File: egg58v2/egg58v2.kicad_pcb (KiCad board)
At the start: 2 copper layers, 146.1 x 146 mm, 32 parts, among them J1 AudioJack4, SW11 SW_PUSH_LED, SW12 SW_PUSH_LED, SW13 SW_PUSH_LED, SW14 SW_PUSH_LED, SW15 SW_PUSH_LED, SW16 SW_PUSH_LED, SW21 SW_PUSH_LED, SW22 SW_PUSH_LED, SW23 SW_PUSH_LED, SW24 SW_PUSH_LED, SW25 SW_PUSH_LED, SW26 SW_PUSH_LED, SW31 SW_PUSH_LED, SW32 SW_PUSH_LED, SW33 SW_PUSH_LED, SW34 SW_PUSH_LED, SW35 SW_PUSH_LED, SW36 SW_PUSH_LED, SW41 SW_PUSH_LED, SW42 SW_PUSH_LED, SW43 SW_PUSH_LED, SW44 SW_PUSH_LED, SW45 SW_PUSH_LED, SW46 SW_PUSH_LED, SW52 SW_PUSH_LED, SW53 SW_PUSH_LED, SW54 SW_PUSH_LED, SW55 SW_PUSH_LED, SW56 SW_PUSH_LED, U1 Elite-C

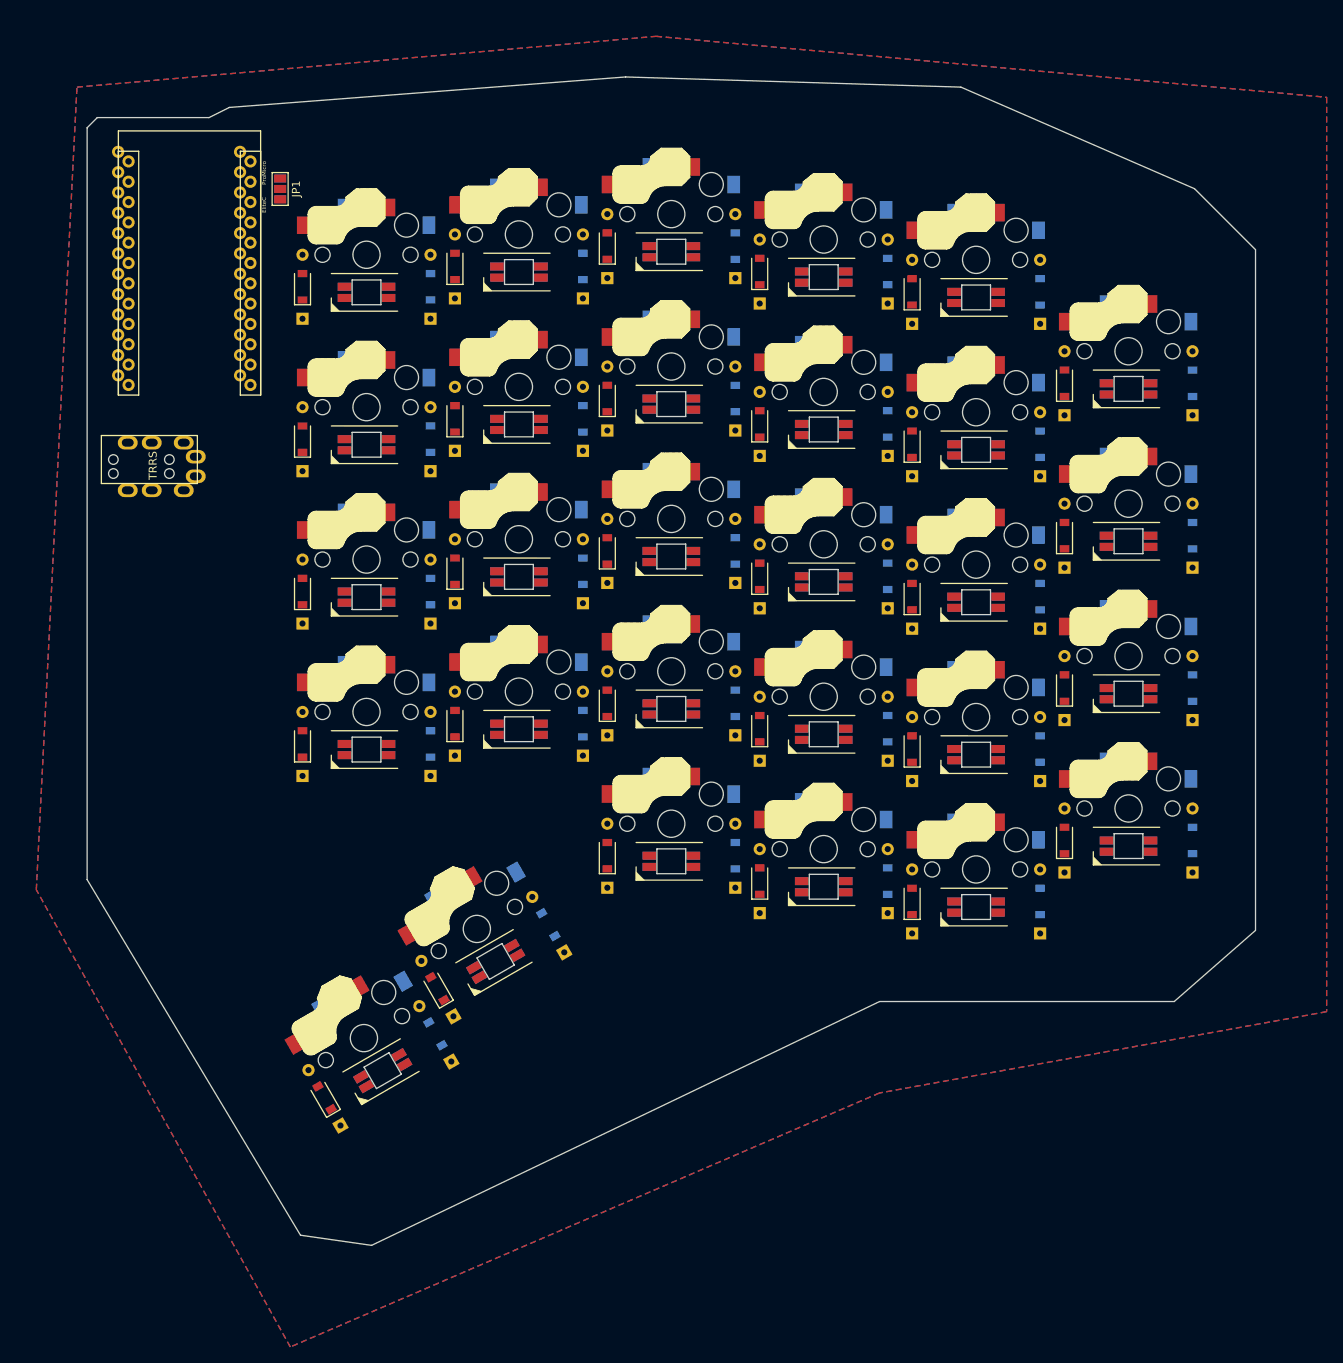
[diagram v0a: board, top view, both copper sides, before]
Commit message: update to choc switch spacing, add logo
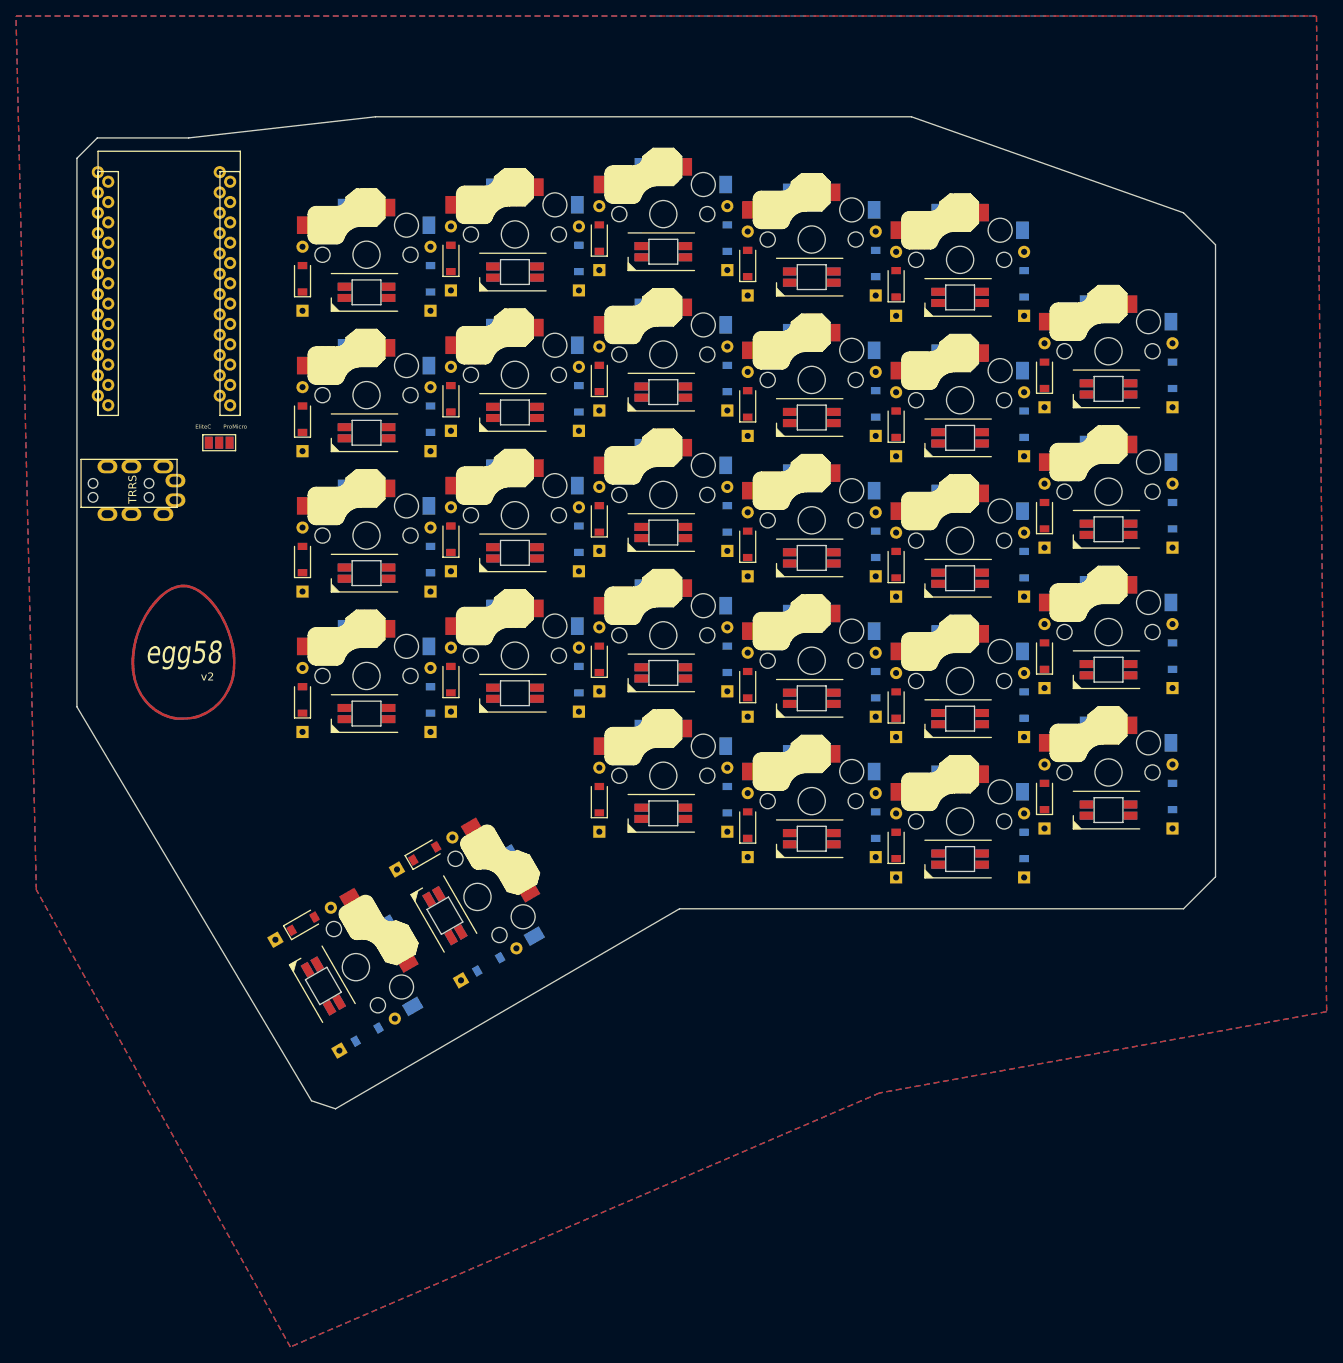
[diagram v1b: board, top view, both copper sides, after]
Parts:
- added G***: LOGO, egg58v2:egg58logo, F.Cu at (120.0, 105.0)
- moved JP1 32.6 mm to (124.5, 78.7), turned to 180 degrees
- moved SW56 8.93 mm to (141.5, 144.3), turned to 300 degrees
- moved SW52 6.32 mm to (217.1, 126.1)
- moved SW53 6.18 mm to (198.5, 123.5)
- moved SW54 6.08 mm to (180.0, 120.4)
- moved SW41 5.15 mm to (235.6, 120.0)
- moved SW42 4.92 mm to (217.1, 108.5)
- moved SW43 4.74 mm to (198.5, 106.0)
- moved SW44 4.61 mm to (180.0, 102.8)
- moved SW45 4.53 mm to (161.4, 105.4)
- moved SW46 4.50 mm to (142.9, 107.9)
- moved SW55 4.00 mm to (156.7, 135.5), turned to 300 degrees
- moved J1 3.92 mm to (107.2, 83.8)
- moved SW31 3.91 mm to (235.6, 102.4)
- moved SW32 3.61 mm to (217.1, 91.0)
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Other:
- board size 146.1 x 146 mm -> 142.3 x 124 mm

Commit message: footprint updates
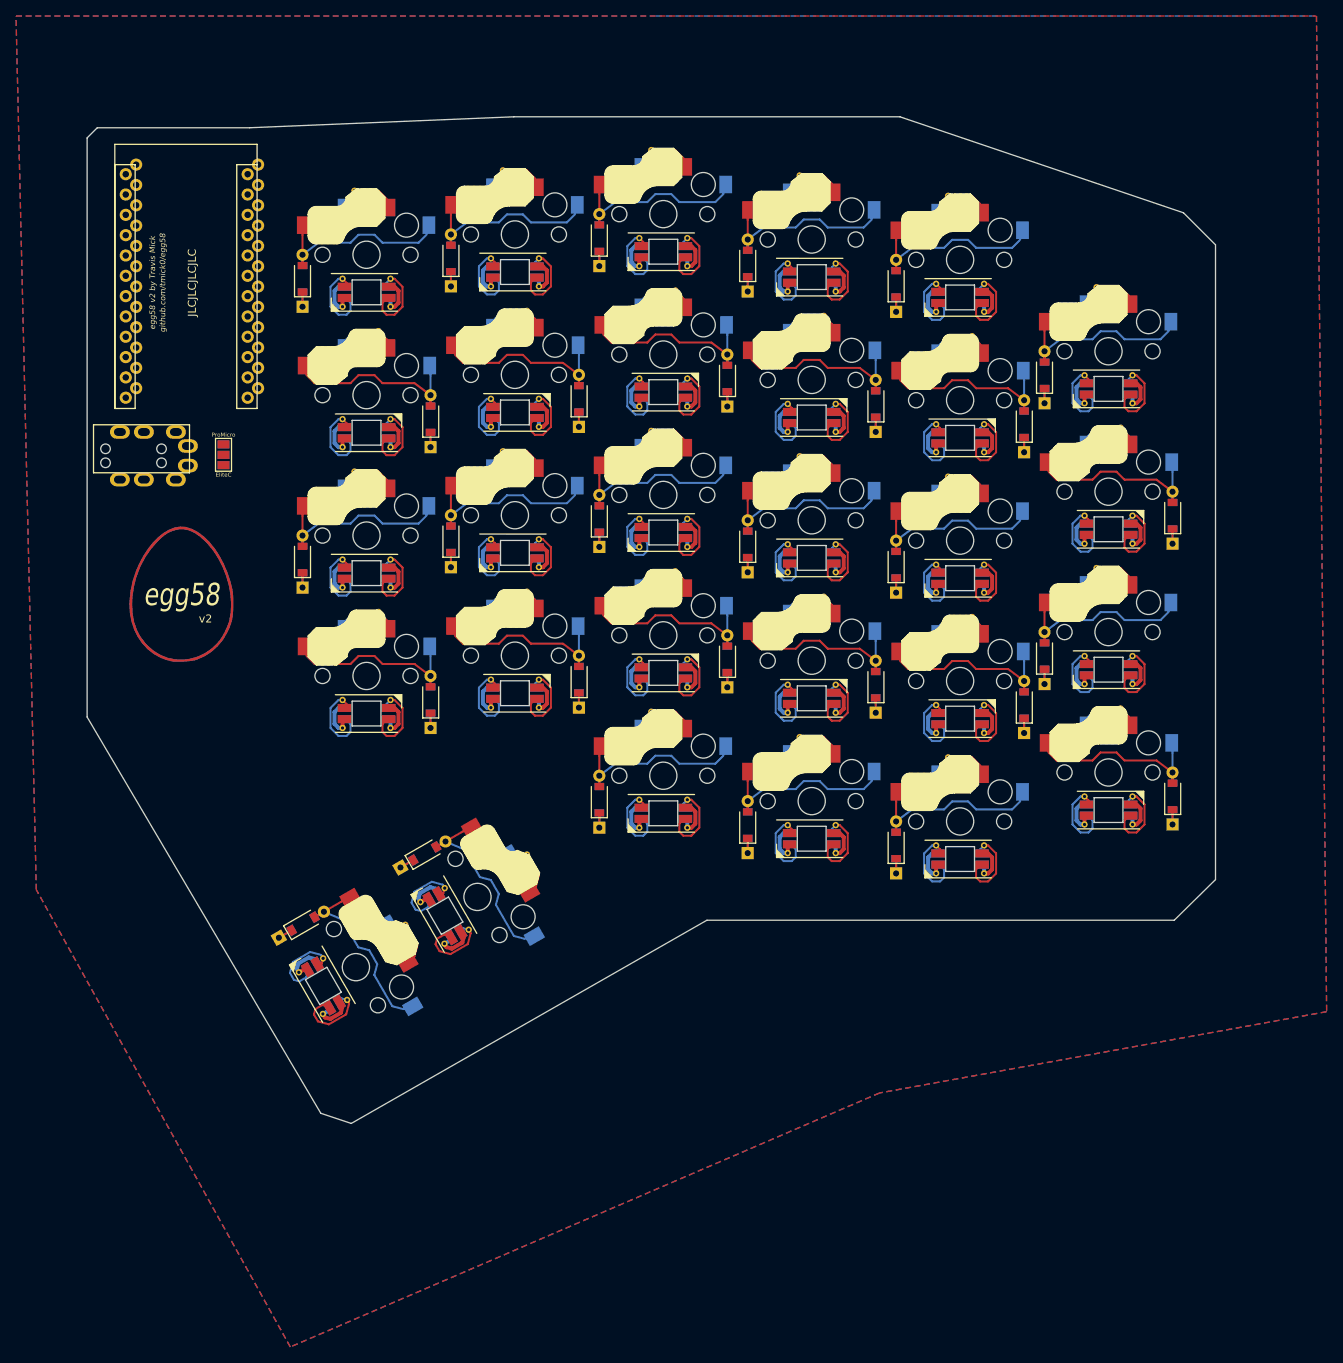
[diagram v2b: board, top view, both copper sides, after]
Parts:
- added REF**: egg58url, egg58v2:egg58url, F.Cu at (116.2, 58.8)
- SW21, SW22, SW23, SW24, SW25, SW26, SW41, SW42, SW43, SW44, SW45, SW46, U1: moved to B.Cu
- moved G*** 7.25 mm to (119.8, 97.8)
- moved J1 4.59 mm to (108.8, 79.5)
- moved U1 2.57 mm to (120.5, 58.8), turned to 180 degrees
- moved JP1 1.60 mm to (125.0, 80.2), turned to 270 degrees
- turned SW21 to 180 degrees
- turned SW22 to 180 degrees
- turned SW23 to 180 degrees
- turned SW24 to 180 degrees
- turned SW25 to 180 degrees
- turned SW26 to 180 degrees
- turned SW41 to 180 degrees
- turned SW42 to 180 degrees
- turned SW43 to 180 degrees
- turned SW44 to 180 degrees
- turned SW45 to 180 degrees
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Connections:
- SW11 pad 5: Net-(SW11-Pad5) -> Col1
- SW11 pad 7: Net-(SW11-Pad6) -> Row1
- SW12 pad 5: Net-(SW12-Pad5) -> Col2
- SW12 pad 7: Net-(SW12-Pad6) -> Row1
- SW13 pad 5: Net-(SW13-Pad5) -> Col3
- SW13 pad 7: Net-(SW13-Pad6) -> Row1
- SW14 pad 5: Net-(SW14-Pad5) -> Col4
- SW14 pad 7: Net-(SW14-Pad6) -> Row1
- SW15 pad 5: Net-(SW15-Pad5) -> Col5
- SW15 pad 7: Net-(SW15-Pad6) -> Row1
- SW16 pad 5: Net-(SW16-Pad5) -> Col6
- SW16 pad 7: Net-(SW16-Pad6) -> Row1
- SW21 pad 5: Net-(SW21-Pad5) -> Col1
- SW21 pad 7: Net-(SW21-Pad6) -> Row2
- SW22 pad 5: Net-(SW22-Pad5) -> Col2
- SW22 pad 7: Net-(SW22-Pad6) -> Row2
- SW23 pad 5: Net-(SW23-Pad5) -> Col3
- SW23 pad 7: Net-(SW23-Pad6) -> Row2
- SW24 pad 5: Net-(SW24-Pad5) -> Col4
- SW24 pad 7: Net-(SW24-Pad6) -> Row2
- SW25 pad 5: Net-(SW25-Pad5) -> Col5
- SW25 pad 7: Net-(SW25-Pad6) -> Row2
- SW26 pad 5: Net-(SW26-Pad5) -> Col6
- SW26 pad 7: Net-(SW26-Pad6) -> Row2
- SW31 pad 5: Net-(SW31-Pad5) -> Col1
- SW31 pad 7: Net-(SW31-Pad6) -> Row3
- SW32 pad 5: Net-(SW32-Pad5) -> Col2
- SW32 pad 7: Net-(SW32-Pad6) -> Row3
- SW33 pad 5: Net-(SW33-Pad5) -> Col3
- SW33 pad 7: Net-(SW33-Pad6) -> Row3
- SW34 pad 5: Net-(SW34-Pad5) -> Col4
- SW34 pad 7: Net-(SW34-Pad6) -> Row3
- SW35 pad 5: Net-(SW35-Pad5) -> Col5
- SW35 pad 7: Net-(SW35-Pad6) -> Row3
- SW36 pad 5: Net-(SW36-Pad5) -> Col6
- SW36 pad 7: Net-(SW36-Pad6) -> Row3
- SW41 pad 7: Net-(SW41-Pad6) -> Row4
- SW42 pad 5: Net-(SW42-Pad5) -> Col2
- SW42 pad 7: Net-(SW42-Pad6) -> Row4
- SW43 pad 5: Net-(SW43-Pad5) -> Col3
- SW43 pad 7: Net-(SW43-Pad6) -> Row4
- SW44 pad 5: Net-(SW44-Pad5) -> Col4
- SW44 pad 7: Net-(SW44-Pad6) -> Row4
- SW45 pad 5: Net-(SW45-Pad5) -> Col5
- SW45 pad 7: Net-(SW45-Pad6) -> Row4
- SW46 pad 5: Net-(SW46-Pad5) -> Col6
- SW46 pad 7: Net-(SW46-Pad6) -> Row4
- SW52 pad 7: Net-(SW52-Pad6) -> Row5
- SW53 pad 7: Net-(SW53-Pad6) -> Row5
- SW54 pad 7: Net-(SW54-Pad6) -> Row5
- SW55 pad 7: Net-(SW55-Pad6) -> Row5
- SW56 pad 7: Net-(SW56-Pad6) -> Row5
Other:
- board size 142.3 x 124 mm -> 141.1 x 125.8 mm

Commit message: make LEDs north facing
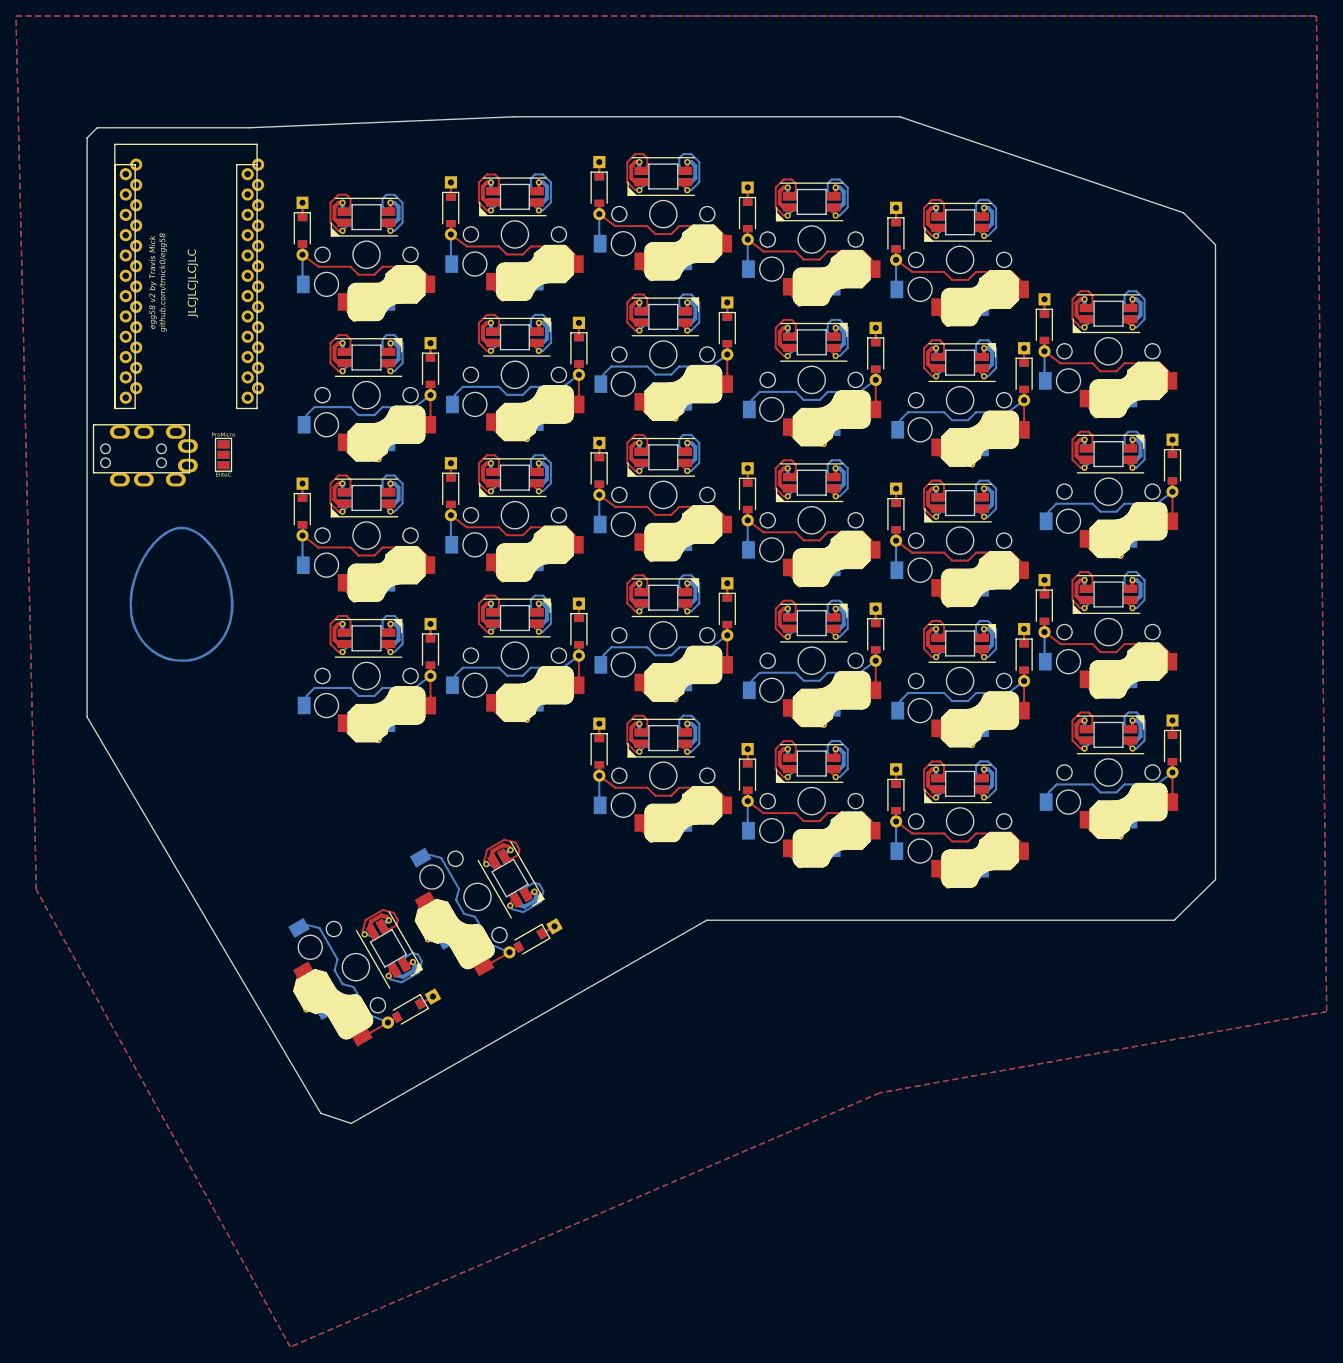
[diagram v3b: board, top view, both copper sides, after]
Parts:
- G***, SW11, SW12, SW13, SW14, SW15, SW16, SW31, SW32, SW33, SW34, SW35, SW36, SW52, SW53, SW54: moved to B.Cu
- SW21, SW22, SW23, SW24, SW25, SW26, SW41, SW42, SW43, SW44, SW45, SW46: moved to F.Cu
- turned G*** to 180 degrees
- turned SW55 to 120 degrees
- turned SW56 to 120 degrees
